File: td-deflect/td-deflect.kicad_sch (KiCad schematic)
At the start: 82 parts, among them J10 Conn_01x02_Male, J11 Conn_01x02_Male, Q1 BSZ42DN25NS3GATMA1, Q10 IPD50R380CE, Q11 IPD50R380CE, Q2 G3R450MT17D, Q3 BSZ42DN25NS3GATMA1, Q4 BCP56, Q5 BCP53, Q6 BD139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

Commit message: add switching heater supply
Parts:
- added R?: 1k, symbol Device:R
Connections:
- net GND: now also R?.2; no longer R12.2
- new net HOT_VOLTAGE: R12.2, R?.1
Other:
- note removed: "todo: add voltage monitoring of h.out"
- note removed: "todo: drop SiC diode and use body diode instead"
- note removed: "todo: swap to lower end SiC"
- moved on the sheet: R12

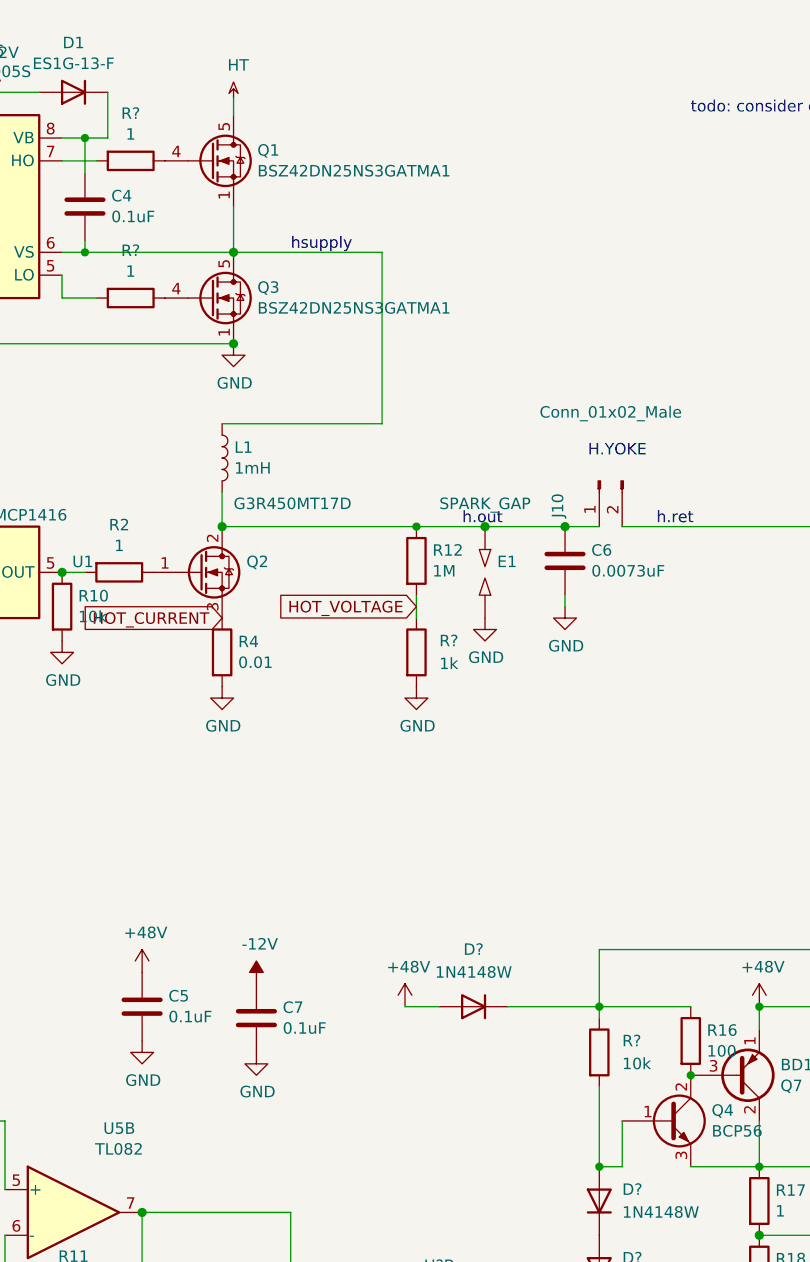
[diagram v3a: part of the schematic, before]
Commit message: switch to stm32g4
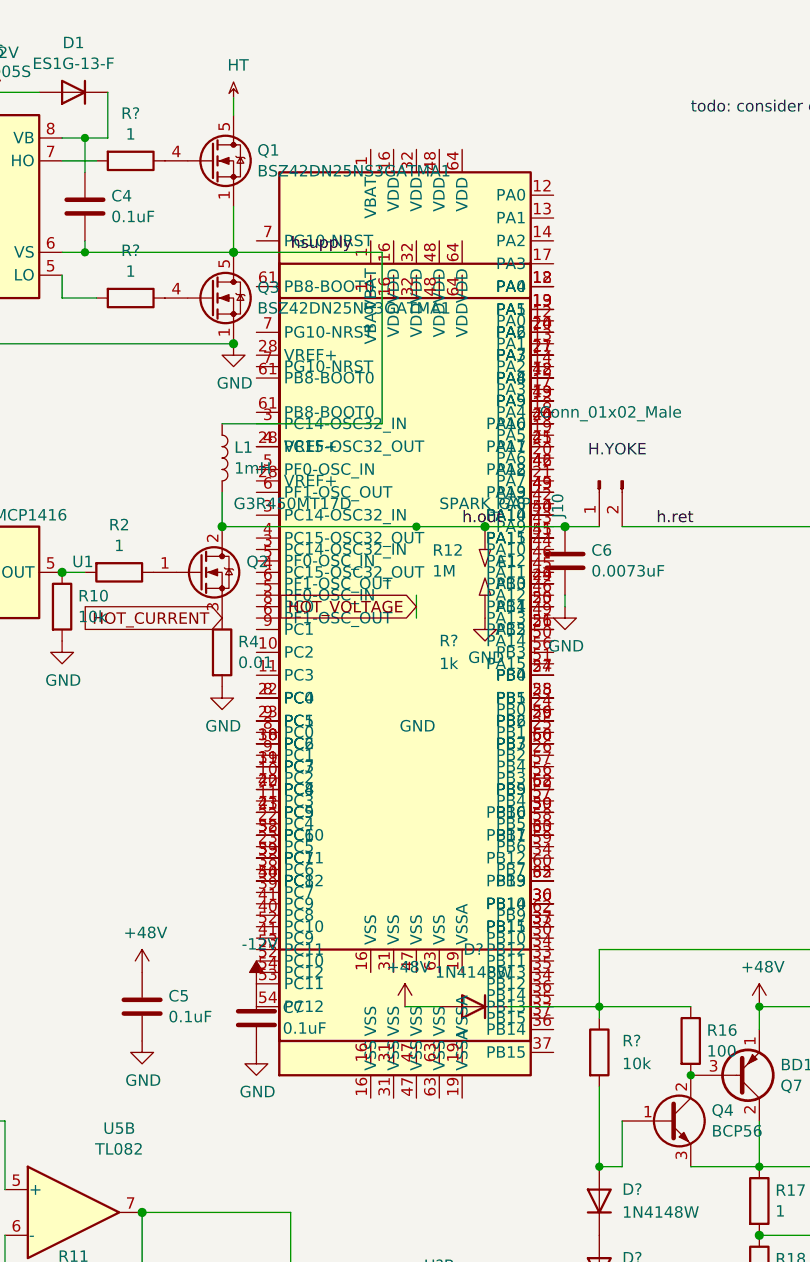
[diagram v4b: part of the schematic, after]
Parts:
- added #PWR0103: GND, Package_QFP:LQFP-64_10x10mm_P0.5mm, symbol td-crt:STM32G474xx
- R12: footprint Resistor_THT:R_Axial_DIN0309_L9.0mm_D3.2mm_P15.24mm_Horizontal -> Package_QFP:LQFP-64_10x10mm_P0.5mm; symbol Device:R -> td-crt:STM32G474xx
- R?: footprint (none) -> Package_QFP:LQFP-64_10x10mm_P0.5mm; symbol Device:R -> td-crt:STM32G474xx
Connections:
- net -12V: now also #PWR0103.53 (PC11)
- net GND: no longer R?.2
- net HOT_VOLTAGE: no longer R12.2, R?.1
- net h.out: no longer R12.1
- new net: R12.18 (PA4), R?.12 (PA0)
- new net: R12.19 (VSSA), R?.13 (PA1)
- new net: R12.20 (PA6), R?.14 (PA2)
- new net: R12.21 (PA7), R?.17 (PA3)
- new net: R12.22 (PC4), R?.8 (PC0)
- new net: R12.23 (PC5), R?.9 (PC1)
- new net: R12.24 (PB0), R?.49 (PA13)
- new net: R12.25 (PB1), R?.50 (PA14)
- new net: R12.26 (PB2), R?.51 (PA15)
- new net: R12.30 (PB10), R?.59 (PB6)
- new net: R12.33 (PB11), R?.60 (PB7)
- new net: R12.35 (PB13), R?.62 (PB9)
- new net: R12.36 (PB14), R?.30 (PB10)
- new net: R12.37 (PB15), R?.33 (PB11)
- new net: R12.38 (PC6), R?.10 (PC2)
- new net: R12.39 (PC7), R?.11 (PC3)
- new net: R12.4 (PC15-OSC32_OUT), R?.28 (VREF+)
- new net: R12.40 (PC8), R?.22 (PC4)
- new net: R12.41 (PC9), R?.23 (PC5)
- new net: R12.42 (PA8), R?.18 (PA4)
- new net: R12.43 (PA9), R?.19 (VSSA)
- new net: R12.44 (PA10), R?.20 (PA6)
- new net: R12.45 (PA11), R?.21 (PA7)
- new net: R12.46 (PA12), R?.42 (PA8)
- new net: R12.49 (PA13), R?.43 (PA9)
- new net: R12.50 (PA14), R?.44 (PA10)
- new net: R12.51 (PA15), R?.45 (PA11)
- new net: R12.52 (PC10), R?.38 (PC6)
- new net: R12.53 (PC11), R?.39 (PC7)
- new net: R12.54 (PC12), R?.40 (PC8)
- new net: R12.57 (PB4), R?.24 (PB0)
- new net: R12.58 (PB5), R?.25 (PB1)
- new net: R12.59 (PB6), R?.26 (PB2)
- new net: R12.60 (PB7), R?.56 (PB3)
- new net: R12.62 (PB9), R?.58 (PB5)
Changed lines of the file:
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@@
     (pin "2")
   )
-  (symbol (lib_id "Device:R") (at 107.95 80.01 0) (unit 1)
+  (symbol (lib_id "td-crt:STM32G474xx") (at 107.95 80.01 0) (unit 1)
     (in_bom yes) (on_board yes)
     (property "Reference" "R12" (id 0) (at 109.728 78.8416 0)
@@
       (effects (font (size 1.27 1.27)) (justify left))
     )
-    (property "Footprint" "Resistor_THT:R_Axial_DIN0309_L9.0mm_D3.2mm_P15.24mm_Horizontal" (id 2) (at 106.172 80.01 90)
-      (effects (font (size 1.27 1.27)) hide)
+    (property "Footprint" "Package_QFP:LQFP-64_10x10mm_P0.5mm" (id 2) (at 92.71 123.19 0)
+      (effects (font (size 1.27 1.27)) (justify right) hide)
     )
-    (property "Datasheet" "~" (id 3) (at 107.95 80.01 0)
+    (property "Datasheet" "https://www.st.com/resource/en/datasheet/stm32g474cb.pdf" (id 3) (at 107.95 80.01 0)
       (effects (font (size 1.27 1.27)) hide)
     )
@@
     )
     (pin "1")
-    (pin "2")
+    (pin "10")
+    (pin "11")
+    (pin "12")
+    (pin "13")
+    (pin "14")
+    (pin "16")
+    (pin "16")
+    (pin "17")
+    (pin "18")
+    (pin "19")
+    (pin "19")
+    (pin "20")
+    (pin "21")
+    (pin "22")
+    (pin "23")
+    (pin "24")
+    (pin "25")
+    (pin "26")
+    (pin "28")
+    (pin "3")
+    (pin "30")
+    (pin "31")
+    (pin "32")
+    (pin "33")
+    (pin "34")
+    (pin "35")
+    (pin "36")
+    (pin "37")
+    (pin "38")
+    (pin "39")
+    (pin "4")
+    (pin "40")
+    (pin "41")
+    (pin "42")
+    (pin "43")
+    (pin "44")
+    (pin "45")
+    (pin "46")
+    (pin "47")
+    (pin "48")
+    (pin "49")
+    (pin "5")
+    (pin "50")
+    (pin "51")
+    (pin "52")
+    (pin "53")
+    (pin "54")
+    (pin "56")
+    (pin "57")
+    (pin "58")
+    (pin "59")
+    (pin "6")
+    (pin "60")
+    (pin "61")
+    (pin "62")
+    (pin "63")
+    (pin "64")
+    (pin "7")
+    (pin "8")
+    (pin "9")
   )
-  (symbol (lib_id "power:GND") (at 107.95 93.98 0) (unit 1)
+  (symbol (lib_id "td-crt:STM32G474xx") (at 107.95 93.98 0) (unit 1)
     (in_bom yes) (on_board yes)
     (property "Reference" "#PWR0103" (id 0) (at 107.95 100.33 0)
@@
     )
     (property "Value" "GND" (id 1) (at 108.077 98.3742 0))
-    (property "Footprint" "" (id 2) (at 107.95 93.98 0)
-      (effects (font (size 1.27 1.27)) hide)
+    (property "Footprint" "Package_QFP:LQFP-64_10x10mm_P0.5mm" (id 2) (at 92.71 137.16 0)
+      (effects (font (size 1.27 1.27)) (justify right) hide)
     )
-    (property "Datasheet" "" (id 3) (at 107.95 93.98 0)
+    (property "Datasheet" "https://www.st.com/resource/en/datasheet/stm32g474cb.pdf" (id 3) (at 107.95 93.98 0)
       (effects (font (size 1.27 1.27)) hide)
     )
     (pin "1")
+    (pin "10")
+    (pin "11")
+    (pin "12")
+    (pin "13")
+    (pin "14")
+    (pin "16")
+    (pin "16")
+    (pin "17")
+    (pin "18")
+    (pin "19")
+    (pin "19")
+    (pin "20")
+    (pin "21")
+    (pin "22")
+    (pin "23")
+    (pin "24")
+    (pin "25")
+    (pin "26")
+    (pin "28")
+    (pin "3")
+    (pin "30")
+    (pin "31")
+    (pin "32")
+    (pin "33")
+    (pin "34")
+    (pin "35")
+    (pin "36")
+    (pin "37")
+    (pin "38")
+    (pin "39")
+    (pin "4")
+    (pin "40")
+    (pin "41")
+    (pin "42")
+    (pin "43")
+    (pin "44")
+    (pin "45")
+    (pin "46")
+    (pin "47")
+    (pin "48")
+    (pin "49")
+    (pin "5")
+    (pin "50")
+    (pin "51")
+    (pin "52")
+    (pin "53")
+    (pin "54")
+    (pin "56")
+    (pin "57")
+    (pin "58")
+    (pin "59")
+    (pin "6")
+    (pin "60")
+    (pin "61")
+    (pin "62")
+    (pin "63")
+    (pin "64")
+    (pin "7")
+    (pin "8")
+    (pin "9")
   )
   (symbol (lib_id "Device:LTRIM") (at 167.64 76.2 90) (unit 1)
@@
     (pin "2")
   )
-  (symbol (lib_id "Device:R") (at 107.95 90.17 0) (unit 1)
+  (symbol (lib_id "td-crt:STM32G474xx") (at 107.95 90.17 0) (unit 1)
     (in_bom yes) (on_board yes) (fields_autoplaced)
     (property "Reference" "R?" (id 0) (at 110.49 88.8999 0)
@@
       (effects (font (size 1.27 1.27)) (justify left))
     )
-    (property "Footprint" "" (id 2) (at 106.172 90.17 90)
-      (effects (font (size 1.27 1.27)) hide)
+    (property "Footprint" "Package_QFP:LQFP-64_10x10mm_P0.5mm" (id 2) (at 92.71 133.35 0)
+      (effects (font (size 1.27 1.27)) (justify right) hide)
     )
-    (property "Datasheet" "~" (id 3) (at 107.95 90.17 0)
+    (property "Datasheet" "https://www.st.com/resource/en/datasheet/stm32g474cb.pdf" (id 3) (at 107.95 90.17 0)
       (effects (font (size 1.27 1.27)) hide)
     )
     (pin "1")
-    (pin "2")
+    (pin "10")
+    (pin "11")
+    (pin "12")
+    (pin "13")
+    (pin "14")
+    (pin "16")
+    (pin "16")
+    (pin "17")
+    (pin "18")
+    (pin "19")
+    (pin "19")
+    (pin "20")
+    (pin "21")
+    (pin "22")
+    (pin "23")
+    (pin "24")
+    (pin "25")
+    (pin "26")
+    (pin "28")
+    (pin "3")
+    (pin "30")
+    (pin "31")
+    (pin "32")
+    (pin "33")
+    (pin "34")
+    (pin "35")
+    (pin "36")
+    (pin "37")
+    (pin "38")
+    (pin "39")
+    (pin "4")
+    (pin "40")
+    (pin "41")
+    (pin "42")
+    (pin "43")
+    (pin "44")
+    (pin "45")
+    (pin "46")
+    (pin "47")
+    (pin "48")
+    (pin "49")
+    (pin "5")
+    (pin "50")
+    (pin "51")
+    (pin "52")
+    (pin "53")
+    (pin "54")
+    (pin "56")
+    (pin "57")
+    (pin "58")
+    (pin "59")
+    (pin "6")
+    (pin "60")
+    (pin "61")
+    (pin "62")
+    (pin "63")
+    (pin "64")
+    (pin "7")
+    (pin "8")
+    (pin "9")
   )
   (symbol (lib_id "Device:R") (at 76.2 35.56 270) (unit 1)
@@
       (reference "#FLG0104") (unit 1) (value "PWR_FLAG") (footprint "")
     )
-    (path "/00000000-0000-0000-0000-00005c37bef7/00000000-0000-0000-0000-00005dc3893a"
-      (reference "#FLG0105") (unit 1) (value "PWR_FLAG") (footprint "")
-    )
     (path "/00000000-0000-0000-0000-00005c37bef7/00000000-0000-0000-0000-00005dc49924"
       (reference "#FLG0106") (unit 1) (value "PWR_FLAG") (footprint "")
@@
     )
     (path "/00000000-0000-0000-0000-00005d9dc04f"
-      (reference "#PWR0103") (unit 1) (value "GND") (footprint "")
+      (reference "#PWR0103") (unit 1) (value "GND") (footprint "Package_QFP:LQFP-64_10x10mm_P0.5mm")
     )
     (path "/00000000-0000-0000-0000-00005d9e8cfb"
@@
       (reference "#PWR0138") (unit 1) (value "GND") (footprint "")
     )
-    (path "/00000000-0000-0000-0000-00005c37bef7/00000000-0000-0000-0000-00005c39e73b"
-      (reference "#PWR0139") (unit 1) (value "GND") (footprint "")
-    )
     (path "/00000000-0000-0000-0000-00005c37bef7/00000000-0000-0000-0000-00005c2ad295"
       (reference "#PWR0140") (unit 1) (value "GND") (footprint "")
@@
       (reference "C34") (unit 1) (value "10uF") (footprint "Capacitor_THT:CP_Radial_D8.0mm_P3.50mm")
     )
-    (path "/00000000-0000-0000-0000-00005c37bef7/00000000-0000-0000-0000-00005c39cb1d"
-      (reference "C35") (unit 1) (value "4.7uF") (footprint "Capacitor_SMD:C_0805_2012Metric_Pad1.15x1.40mm_HandSolder")
-    )
     (path "/00000000-0000-0000-0000-00005c37bef7/00000000-0000-0000-0000-00005c3802f3"
       (reference "C36") (unit 1) (value "0.1uF") (footprint "Capacitor_SMD:C_0805_2012Metric_Pad1.15x1.40mm_HandSolder")
@@
     )
     (path "/00000000-0000-0000-0000-00005d9dc03e"
-      (reference "R12") (unit 1) (value "1M") (footprint "Resistor_THT:R_Axial_DIN0309_L9.0mm_D3.2mm_P15.24mm_Horizontal")
+      (reference "R12") (unit 1) (value "1M") (footprint "Package_QFP:LQFP-64_10x10mm_P0.5mm")
     )
     (path "/00000000-0000-0000-0000-00005da3fc3d"
@@
     )
     (path "/8ecd6c25-c396-401e-b4b6-ed2e882a41fb"
-      (reference "R?") (unit 1) (value "1k") (footprint "")
+      (reference "R?") (unit 1) (value "1k") (footprint "Package_QFP:LQFP-64_10x10mm_P0.5mm")
     )
     (path "/956604f0-4169-43b1-9fb2-4fdc32823a3c"

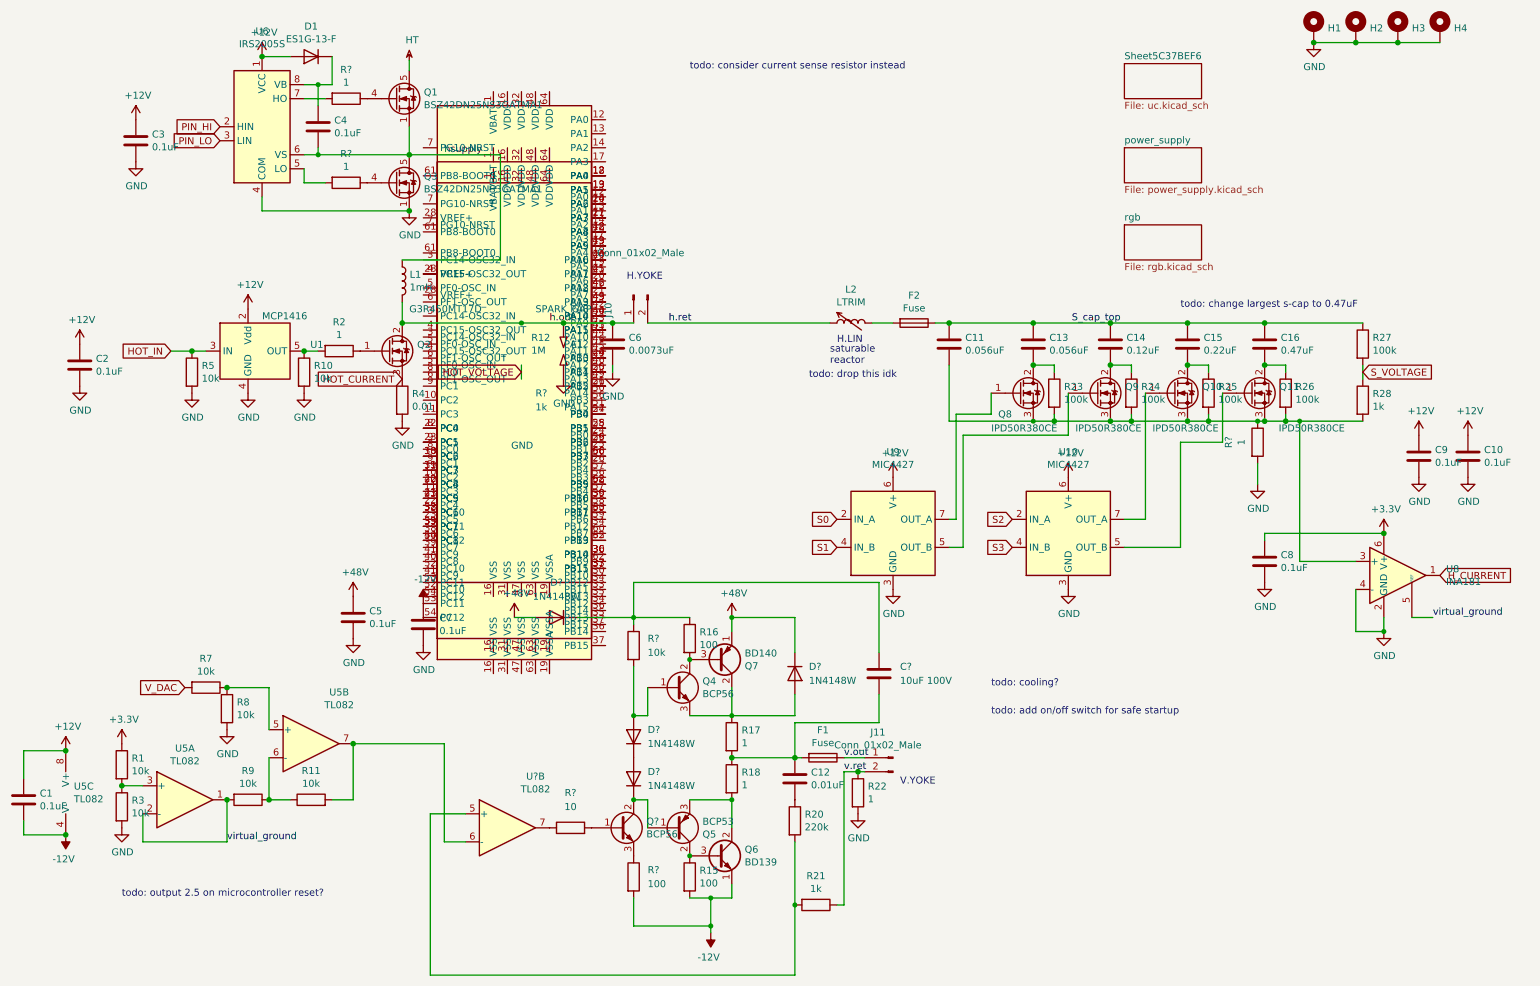
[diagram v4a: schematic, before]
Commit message: current measurement for h
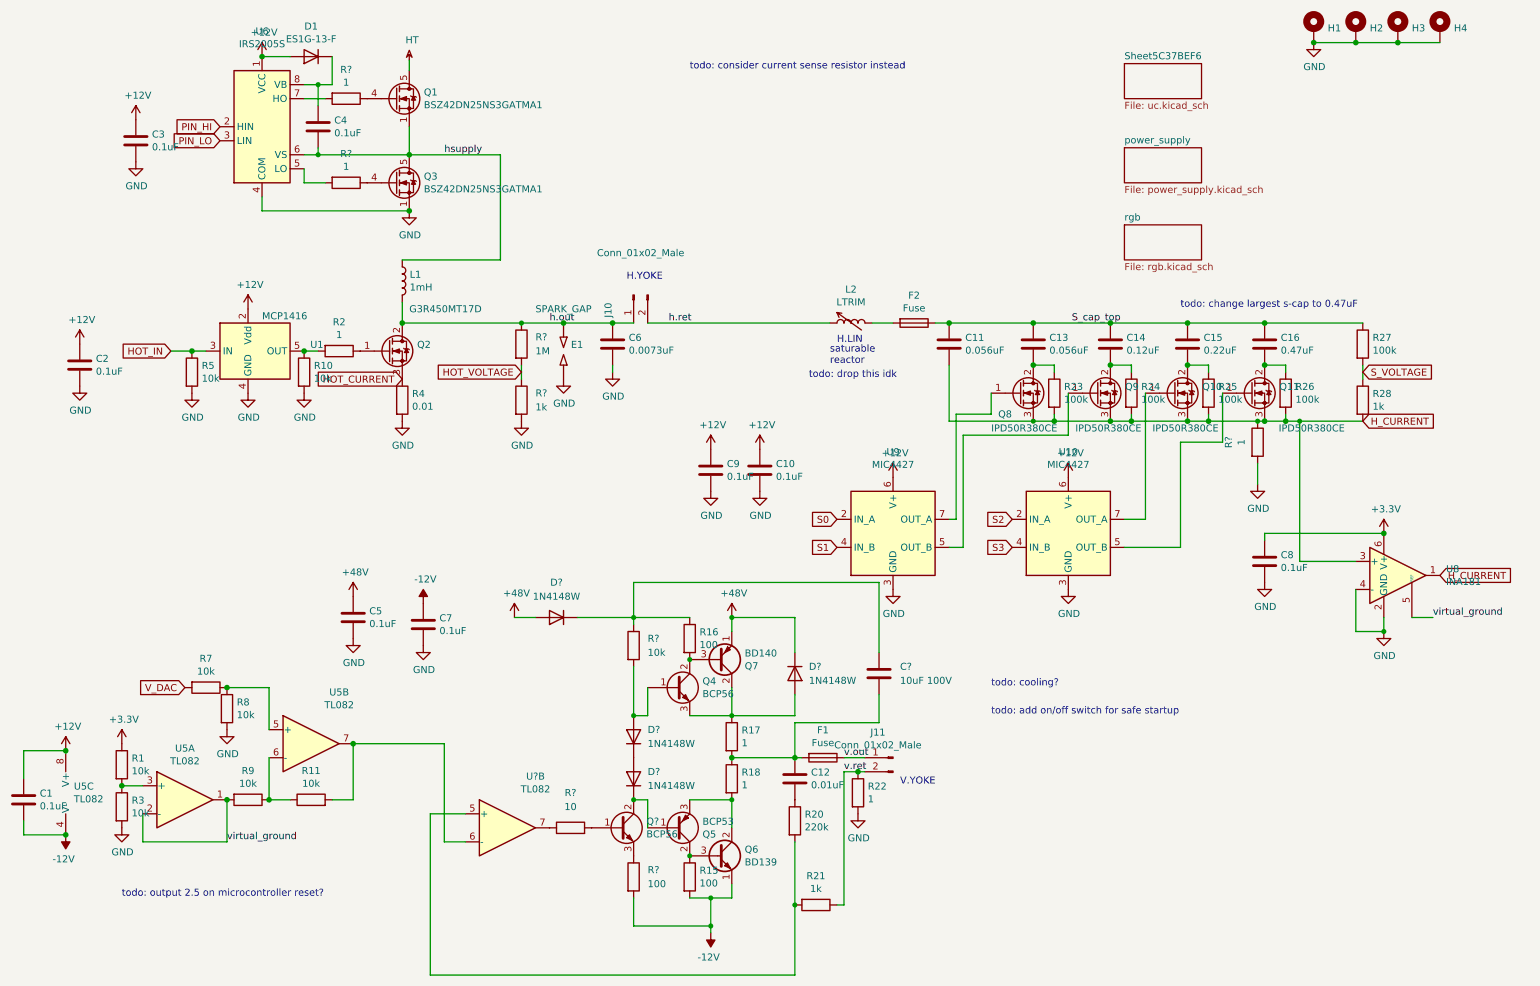
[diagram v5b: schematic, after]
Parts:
- removed #PWR0103: GND, Package_QFP:LQFP-64_10x10mm_P0.5mm, symbol td-crt:STM32G474xx
- removed R12: 1M, Package_QFP:LQFP-64_10x10mm_P0.5mm, symbol td-crt:STM32G474xx
- removed R?: 1k, Package_QFP:LQFP-64_10x10mm_P0.5mm, symbol td-crt:STM32G474xx
- added R?: 1M, symbol Device:R
- added R?: 1k, symbol Device:R
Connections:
- net GND: now also R?.2
- net HOT_VOLTAGE: now also R?.1, R?.2
- net H_CURRENT: now also C11.2, Q10.3 (S), Q11.3 (S), Q8.3 (S), Q9.3 (S), R23.2, R24.2, R25.2, R26.2, R28.2, R?.1, U8.3 (+)
- net h.out: now also R?.1
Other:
- moved on the sheet: C10, C9
